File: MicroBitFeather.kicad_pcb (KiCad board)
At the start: 2 copper layers, 67.3 x 35.6 mm, 16 parts, among them J1 Feather_Long, J2 Barrel_Jack_MountingPin, J3 Feather_Short, J4 NeoPixels, J5 microbit_edge_connector, U1 74AHCT125, U2 MCP1702-3302E_TO92

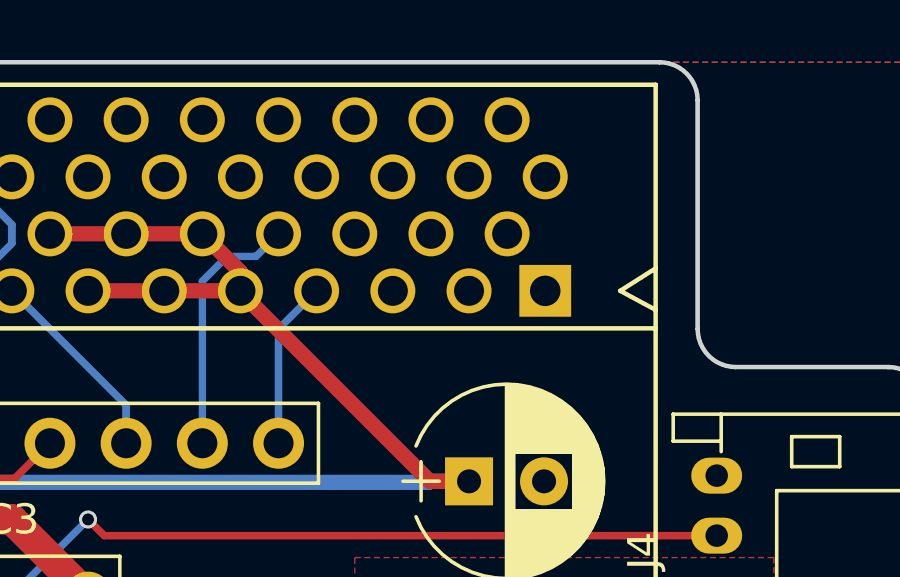
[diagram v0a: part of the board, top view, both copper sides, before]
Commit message: Passes DRC now.
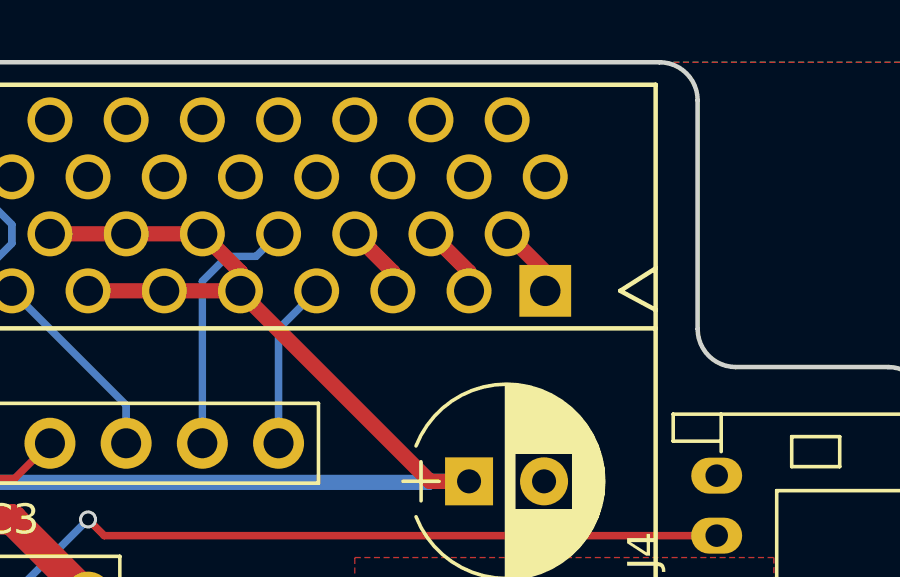
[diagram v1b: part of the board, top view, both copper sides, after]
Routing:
- net GND: track 0.00 -> 7.28 mm
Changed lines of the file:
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@@
   (general
     (links 79)
-    (no_connects 3)
+    (no_connects 0)
     (area 118.034999 83.744999 185.495001 119.455001)
     (thickness 1.6)
     (drawings 12)
-    (tracks 273)
+    (tracks 279)
     (zones 0)
     (modules 16)
@@
   )
   (setup
-    (last_trace_width 0.25)
+    (last_trace_width 0.508)
     (user_trace_width 0.508)
     (user_trace_width 1.016)
@@
   (segment (start 159.909 101.6) (end 158.61137 101.6) (width 1.016) (layer F.Cu) (net 1))
   (segment (start 158.61137 101.6) (end 157.48 101.6) (width 1.016) (layer F.Cu) (net 1))
+  (segment (start 172.72 91.44) (end 172.72 90.81) (width 0.508) (layer F.Cu) (net 2))
+  (segment (start 172.72 90.81) (end 171.45 89.54) (width 0.508) (layer F.Cu) (net 2))
+  (segment (start 170.18 91.44) (end 170.18 90.81) (width 0.508) (layer F.Cu) (net 2))
+  (segment (start 170.18 90.81) (end 168.91 89.54) (width 0.508) (layer F.Cu) (net 2))
+  (segment (start 167.64 91.44) (end 167.64 90.81) (width 0.508) (layer F.Cu) (net 2))
+  (segment (start 167.64 90.81) (end 166.37 89.54) (width 0.508) (layer F.Cu) (net 2))
   (segment (start 156.21 110.49) (end 149.86 110.49) (width 0.508) (layer F.Cu) (net 3))
   (segment (start 149.86 110.49) (end 149.789999 110.560001) (width 0.508) (layer F.Cu) (net 3))

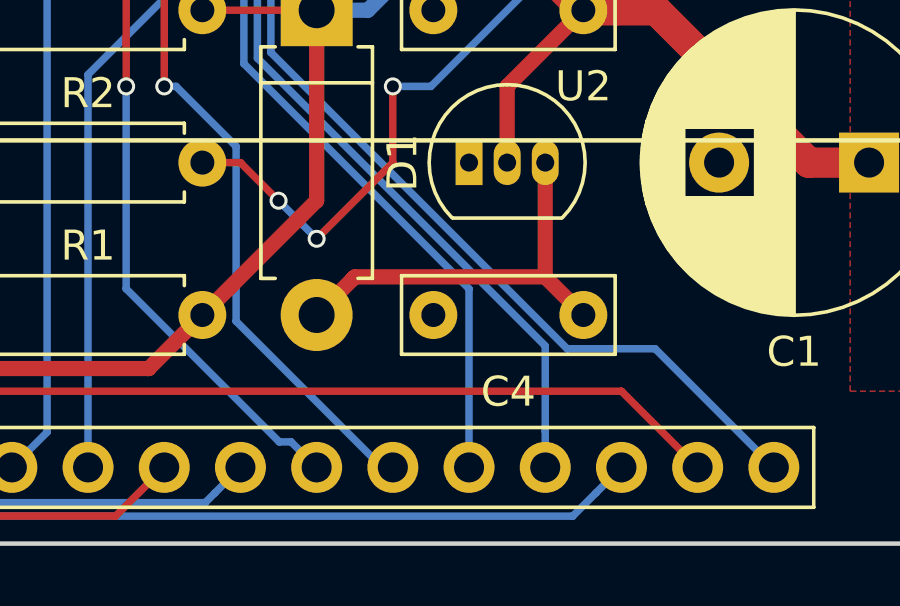
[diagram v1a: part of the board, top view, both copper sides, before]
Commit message: Move one wire to help GND routing a little bit.
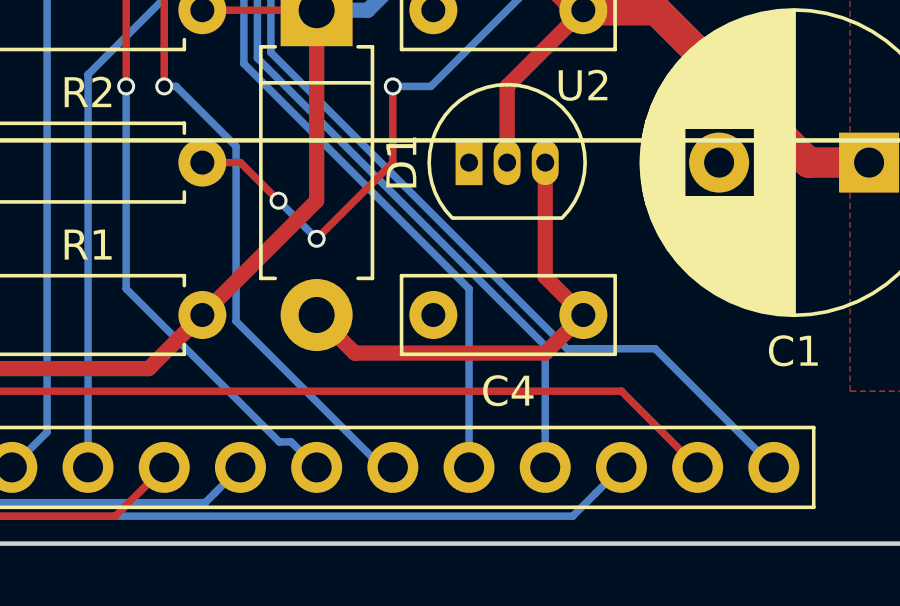
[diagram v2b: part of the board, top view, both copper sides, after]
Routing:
- net Net-(C4-Pad1): track 13.8 -> 15.5 mm
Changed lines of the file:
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@@
   (segment (start 167.64 91.44) (end 167.64 90.81) (width 0.508) (layer F.Cu) (net 2))
   (segment (start 167.64 90.81) (end 166.37 89.54) (width 0.508) (layer F.Cu) (net 2))
-  (segment (start 156.21 110.49) (end 149.86 110.49) (width 0.508) (layer F.Cu) (net 3))
-  (segment (start 149.86 110.49) (end 149.789999 110.560001) (width 0.508) (layer F.Cu) (net 3))
-  (segment (start 149.789999 110.560001) (end 148.59 111.76) (width 0.508) (layer F.Cu) (net 3))
+  (segment (start 156.21 113.03) (end 149.86 113.03) (width 0.508) (layer F.Cu) (net 3))
+  (segment (start 149.86 113.03) (end 148.59 111.76) (width 0.508) (layer F.Cu) (net 3))
+  (segment (start 157.48 111.76) (end 156.21 113.03) (width 0.508) (layer F.Cu) (net 3))
   (segment (start 156.21 106.68) (end 156.21 110.49) (width 0.508) (layer F.Cu) (net 3))
   (segment (start 156.21 110.49) (end 157.48 111.76) (width 0.508) (layer F.Cu) (net 3))

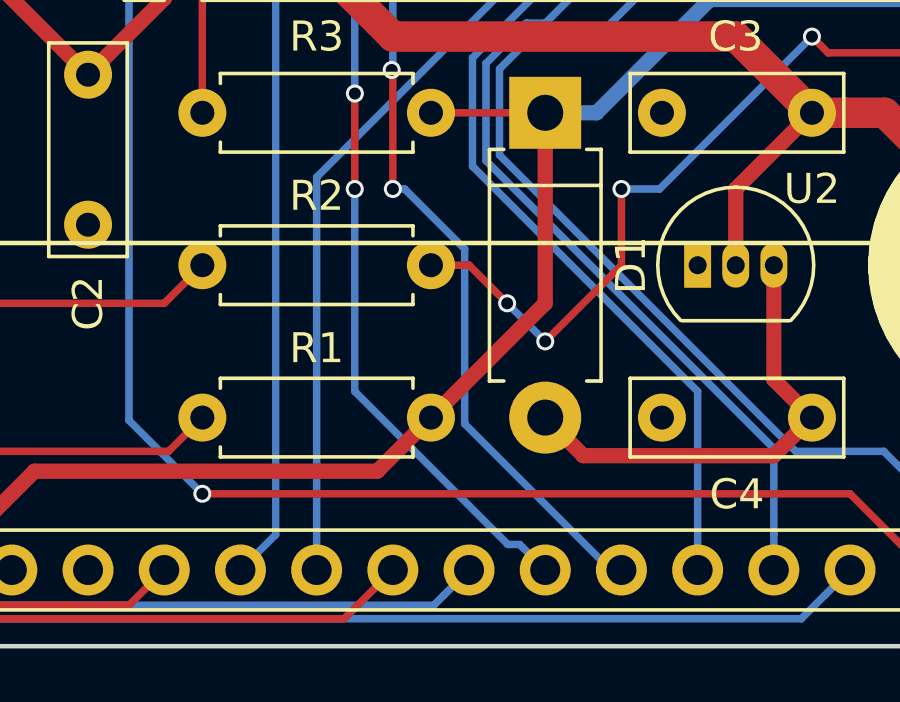
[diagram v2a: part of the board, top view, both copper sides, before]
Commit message: Some stitching vias should help GND.
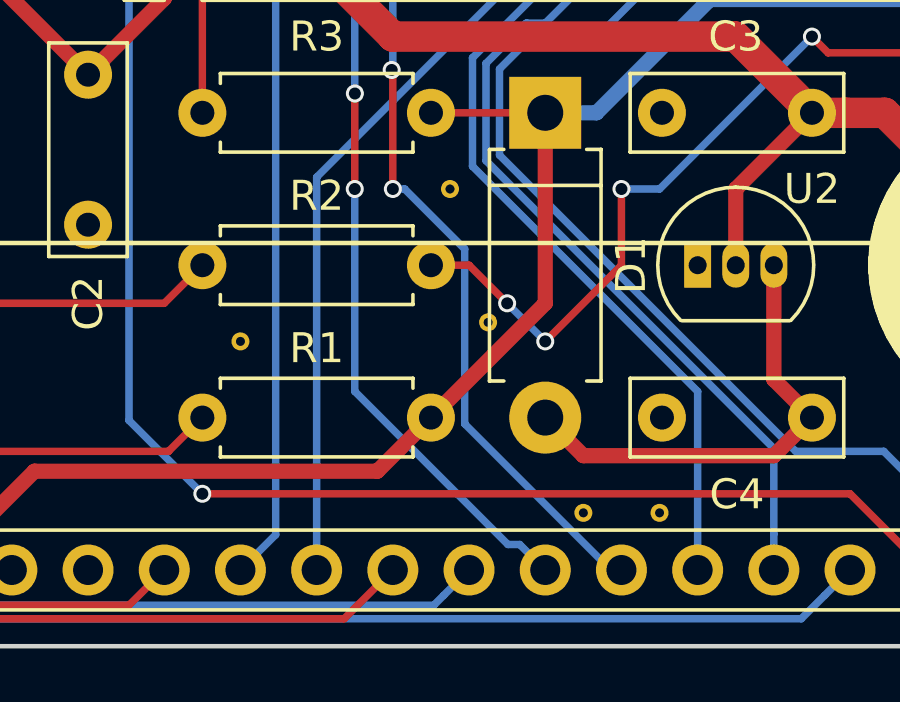
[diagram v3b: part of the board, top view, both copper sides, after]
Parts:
- added VIA: VIA-0.6mm, footprints:VIA-0.6mm, F.Cu at (145.4, 104.1)
- added VIA: VIA-0.6mm, footprints:VIA-0.6mm, F.Cu at (138.4, 109.2)
- added VIA: VIA-0.6mm, footprints:VIA-0.6mm, F.Cu at (146.7, 108.6)
- added VIA: VIA-0.6mm, footprints:VIA-0.6mm, F.Cu at (149.9, 114.9)
- added VIA: VIA-0.6mm, footprints:VIA-0.6mm, F.Cu at (152.4, 114.9)
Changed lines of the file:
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@@
 (kicad_pcb (version 4) (host pcbnew 4.0.7)
   (general
-    (links 79)
+    (links 84)
     (no_connects 0)
-    (area 118.034999 83.744999 185.495001 119.455001)
+    (area 118.034999 79.965 186.795 121.968572)
     (thickness 1.6)
     (drawings 12)
     (tracks 279)
     (zones 0)
-    (modules 16)
+    (modules 21)
     (nets 72)
   )
@@
   )
   (setup
-    (last_trace_width 0.508)
+    (last_trace_width 0.25)
     (user_trace_width 0.508)
     (user_trace_width 1.016)
@@
     (mod_text_size 1 1)
     (mod_text_width 0.15)
-    (pad_size 1.524 1.524)
-    (pad_drill 0.762)
+    (pad_size 0.6 0.6)
+    (pad_drill 0.3)
     (pad_to_mask_clearance 0)
     (aux_axis_origin 0 0)
@@
     (add_net "Net-(U1-Pad6)")
     (add_net "Net-(U1-Pad8)")
+  )
+  (module footprints:VIA-0.6mm (layer F.Cu)
+    (at 145.415 104.14)
+    (fp_text reference VIA (at 0 0.5) (layer F.SilkS) hide
+      (effects (font (size 0.127 0.127) (thickness 0.015)))
+    )
+    (fp_text value VIA-0.6mm (at 0 -0.5) (layer F.Fab) hide
+      (effects (font (size 0.127 0.127) (thickness 0.015)))
+    )
+    (pad 1 thru_hole circle (at 0 0) (size 0.6 0.6) (drill 0.3) (layers *.Cu)
+      (net 2 GND) (zone_connect 2))
+  )
+  (module footprints:VIA-0.6mm (layer F.Cu)
+    (at 138.43 109.22)
+    (fp_text reference VIA (at 0 0.5) (layer F.SilkS) hide
+      (effects (font (size 0.127 0.127) (thickness 0.015)))
+    )
+    (fp_text value VIA-0.6mm (at 0 -0.5) (layer F.Fab) hide
+      (effects (font (size 0.127 0.127) (thickness 0.015)))
+    )
+    (pad 1 thru_hole circle (at 0 0) (size 0.6 0.6) (drill 0.3) (layers *.Cu)
+      (net 2 GND) (zone_connect 2))
+  )
+  (module footprints:VIA-0.6mm (layer F.Cu)
+    (at 146.685 108.585)
+    (fp_text reference VIA (at 0 0.5) (layer F.SilkS) hide
+      (effects (font (size 0.127 0.127) (thickness 0.015)))
+    )
+    (fp_text value VIA-0.6mm (at 0 -0.5) (layer F.Fab) hide
+      (effects (font (size 0.127 0.127) (thickness 0.015)))
+    )
+    (pad 1 thru_hole circle (at 0 0) (size 0.6 0.6) (drill 0.3) (layers *.Cu)
+      (net 2 GND) (zone_connect 2))
+  )
+  (module footprints:VIA-0.6mm (layer F.Cu)
+    (at 149.86 114.935)
+    (fp_text reference VIA (at 0 0.5) (layer F.SilkS) hide
+      (effects (font (size 0.127 0.127) (thickness 0.015)))
+    )
+    (fp_text value VIA-0.6mm (at 0 -0.5) (layer F.Fab) hide
+      (effects (font (size 0.127 0.127) (thickness 0.015)))
+    )
+    (pad 1 thru_hole circle (at 0 0) (size 0.6 0.6) (drill 0.3) (layers *.Cu)
+      (net 2 GND) (zone_connect 2))
   )
   (module Capacitors_THT:CP_Radial_D10.0mm_P5.00mm (layer F.Cu)
@@
     )
   )
+  (module footprints:VIA-0.6mm (layer F.Cu)
+    (at 152.4 114.935)
+    (fp_text reference VIA (at 0 0.5) (layer F.SilkS) hide
+      (effects (font (size 0.127 0.127) (thickness 0.015)))
+    )
+    (fp_text value VIA-0.6mm (at 0 -0.5) (layer F.Fab) hide
+      (effects (font (size 0.127 0.127) (thickness 0.015)))
+    )
+    (pad 1 thru_hole circle (at 0 0) (size 0.6 0.6) (drill 0.3) (layers *.Cu)
+      (net 2 GND) (zone_connect 2))
+  )
   (gr_line (start 176.53 83.82) (end 119.38 83.82) (angle 90) (layer Edge.Cuts) (width 0.15))

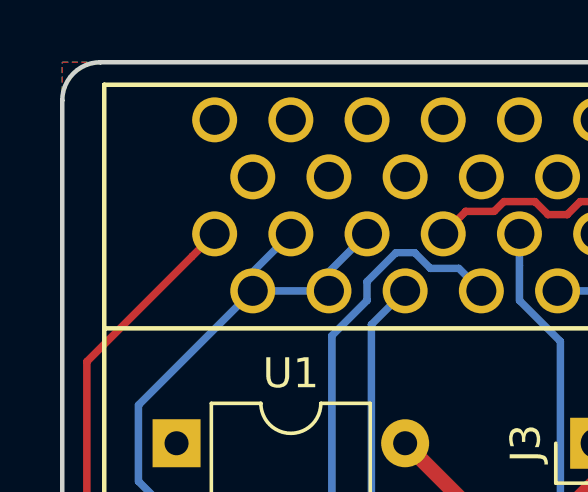
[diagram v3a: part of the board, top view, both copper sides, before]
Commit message: One more stitching via.
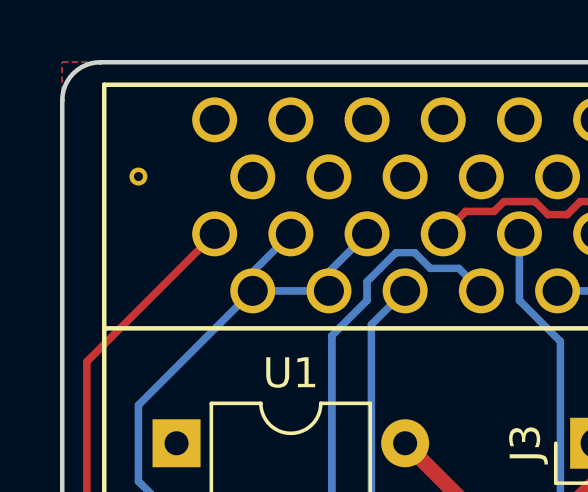
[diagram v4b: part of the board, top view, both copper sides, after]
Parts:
- added VIA: VIA-0.6mm, footprints:VIA-0.6mm, F.Cu at (120.7, 87.6)
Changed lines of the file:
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@@
 (kicad_pcb (version 4) (host pcbnew 4.0.7)
   (general
-    (links 84)
+    (links 85)
     (no_connects 0)
     (area 118.034999 79.965 186.795 121.968572)
@@
     (tracks 279)
     (zones 0)
-    (modules 21)
+    (modules 22)
     (nets 72)
   )
   (page USLetter)
+  (title_block
+    (date 2018-08-30)
+    (company "Patrick Pelletier")
+  )
   (layers
     (0 F.Cu signal)
@@
   )
   (module footprints:VIA-0.6mm (layer F.Cu)
+    (at 120.65 87.63)
+    (fp_text reference VIA (at 0 0.5) (layer F.SilkS) hide
+      (effects (font (size 0.127 0.127) (thickness 0.015)))
+    )
+    (fp_text value VIA-0.6mm (at 0 -0.5) (layer F.Fab) hide
+      (effects (font (size 0.127 0.127) (thickness 0.015)))
+    )
+    (pad 1 thru_hole circle (at 0 0) (size 0.6 0.6) (drill 0.3) (layers *.Cu)
+      (net 2 GND) (zone_connect 2))
+  )
+  (module footprints:VIA-0.6mm (layer F.Cu)

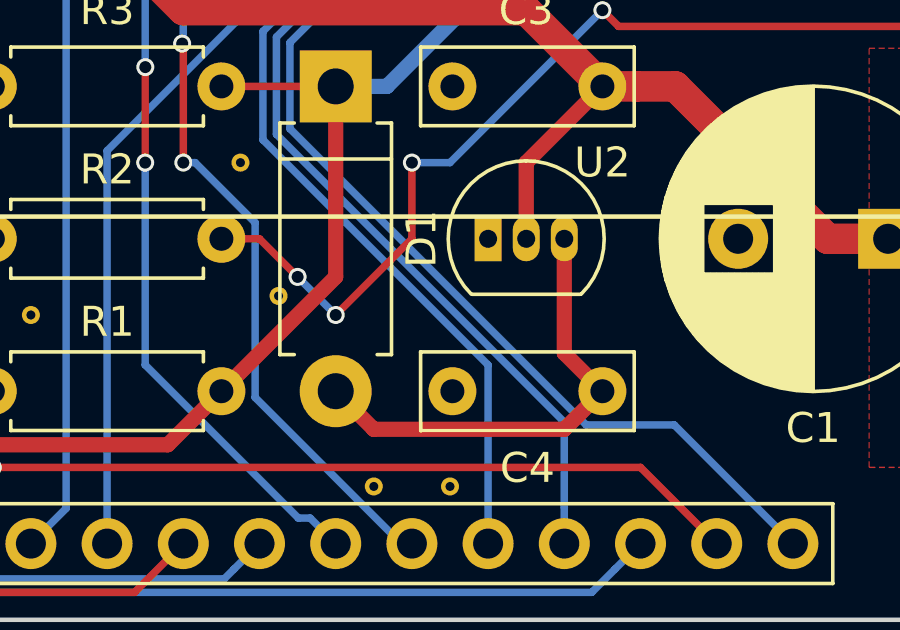
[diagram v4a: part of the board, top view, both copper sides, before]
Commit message: Add a couple more stiching vias.
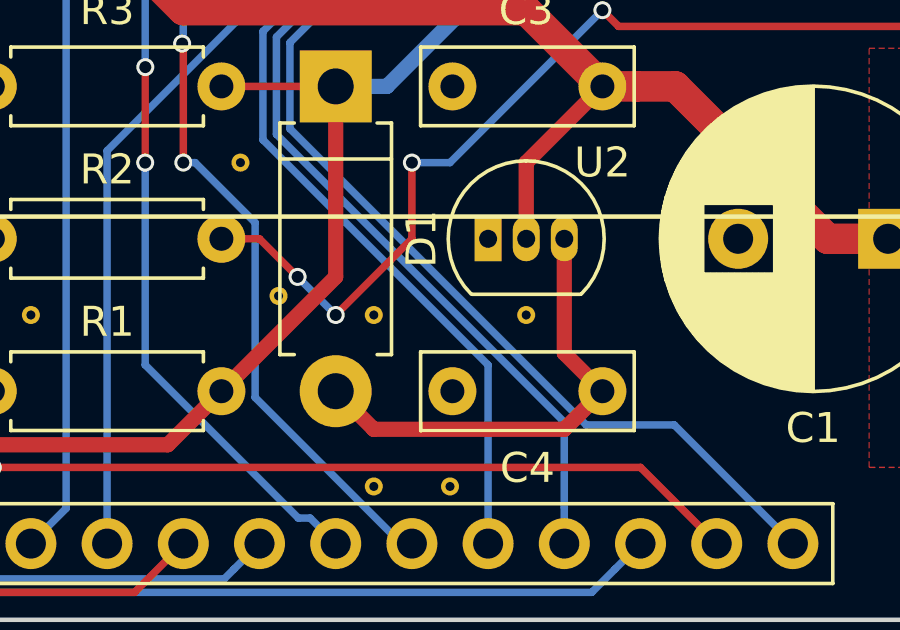
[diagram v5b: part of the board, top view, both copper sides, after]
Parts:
- added VIA: VIA-0.6mm, footprints:VIA-0.6mm, F.Cu at (154.9, 109.2)
- added VIA: VIA-0.6mm, footprints:VIA-0.6mm, F.Cu at (149.9, 109.2)
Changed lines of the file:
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@@
 (kicad_pcb (version 4) (host pcbnew 4.0.7)
   (general
-    (links 85)
+    (links 87)
     (no_connects 0)
     (area 118.034999 79.965 186.795 121.968572)
@@
     (tracks 279)
     (zones 0)
-    (modules 22)
+    (modules 24)
     (nets 72)
   )
@@
   )
   (module footprints:VIA-0.6mm (layer F.Cu)
+    (at 154.94 109.22)
+    (fp_text reference VIA (at 0 0.5) (layer F.SilkS) hide
+      (effects (font (size 0.127 0.127) (thickness 0.015)))
+    )
+    (fp_text value VIA-0.6mm (at 0 -0.5) (layer F.Fab) hide
+      (effects (font (size 0.127 0.127) (thickness 0.015)))
+    )
+    (pad 1 thru_hole circle (at 0 0) (size 0.6 0.6) (drill 0.3) (layers *.Cu)
+      (net 2 GND) (zone_connect 2))
+  )
+  (module footprints:VIA-0.6mm (layer F.Cu)
+    (at 149.86 109.22)
+    (fp_text reference VIA (at 0 0.5) (layer F.SilkS) hide
+      (effects (font (size 0.127 0.127) (thickness 0.015)))
+    )
+    (fp_text value VIA-0.6mm (at 0 -0.5) (layer F.Fab) hide
+      (effects (font (size 0.127 0.127) (thickness 0.015)))
+    )
+    (pad 1 thru_hole circle (at 0 0) (size 0.6 0.6) (drill 0.3) (layers *.Cu)
+      (net 2 GND) (zone_connect 2))
+  )
+  (module footprints:VIA-0.6mm (layer F.Cu)
